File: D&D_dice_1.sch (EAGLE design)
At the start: 29 parts, among them IC1 MCP6282-E/SN-ND, SW1 SPST_SWITCH, SW2 SPST_SWITCH, SW3 SPST_SWITCH, SW4 SPST_SWITCH, SW5 SPST_SWITCH, SW6 SPST_SWITCH, U1 ATMEGA168

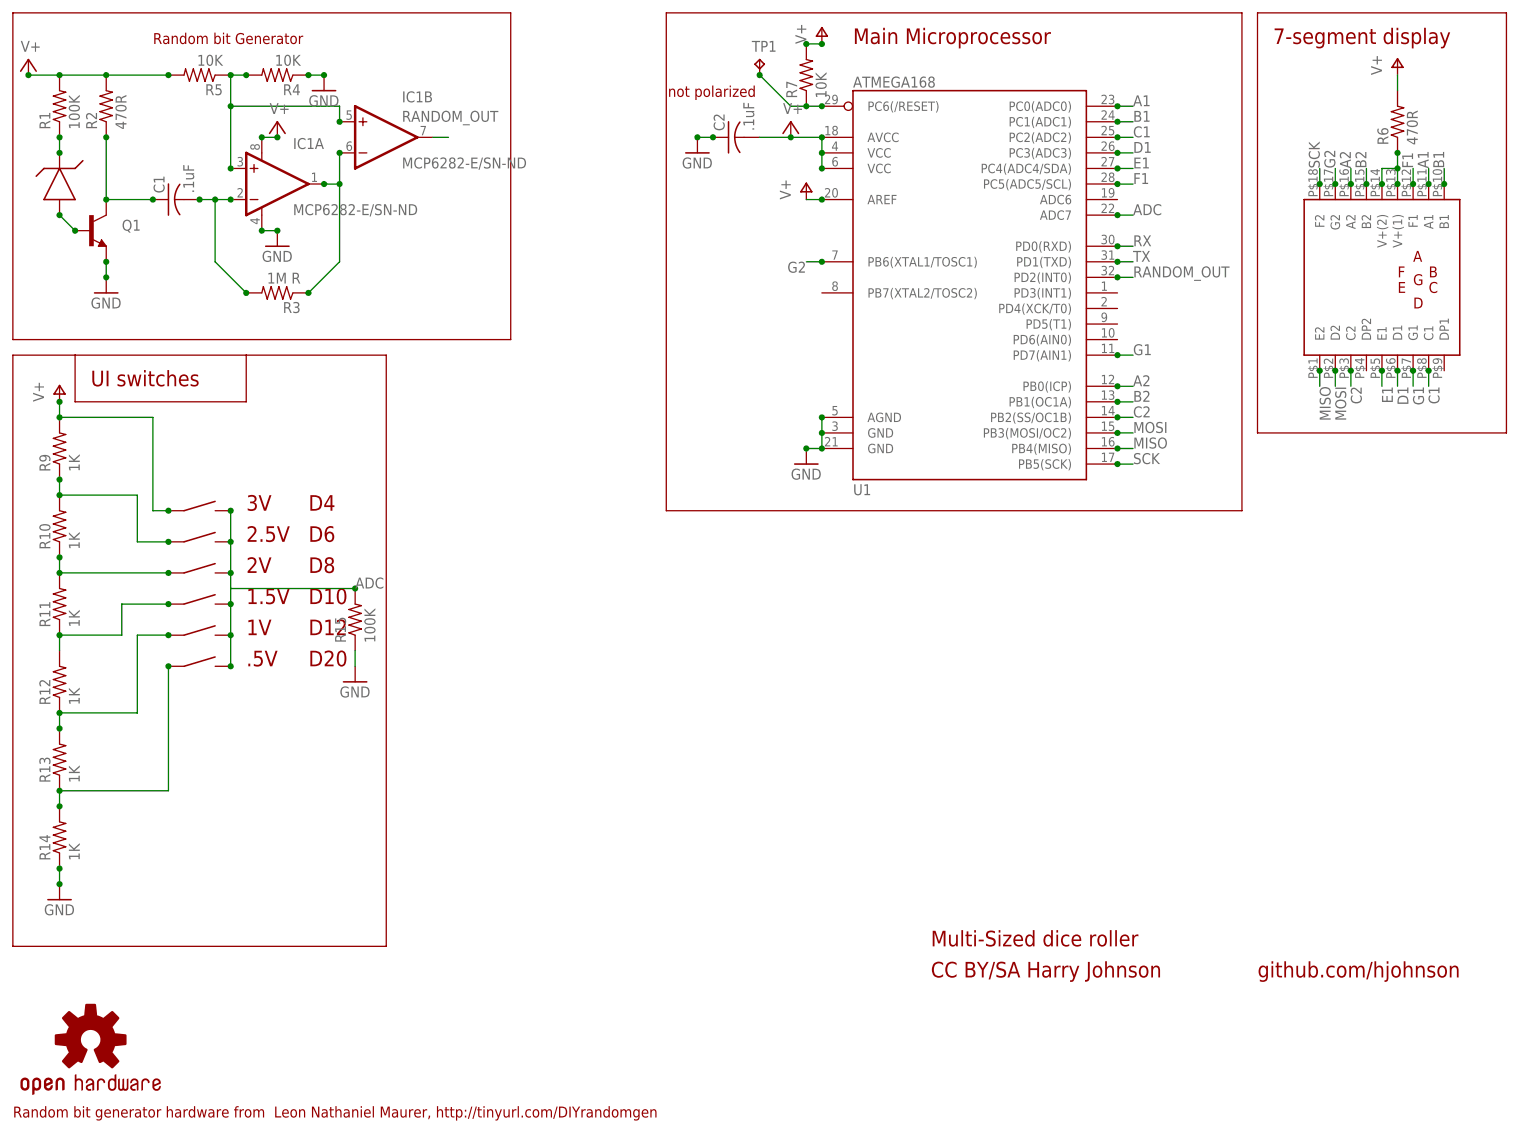
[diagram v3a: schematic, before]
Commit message: Added a whole bunch of explanatory text to the schematic.
Theory of operation, mainly.
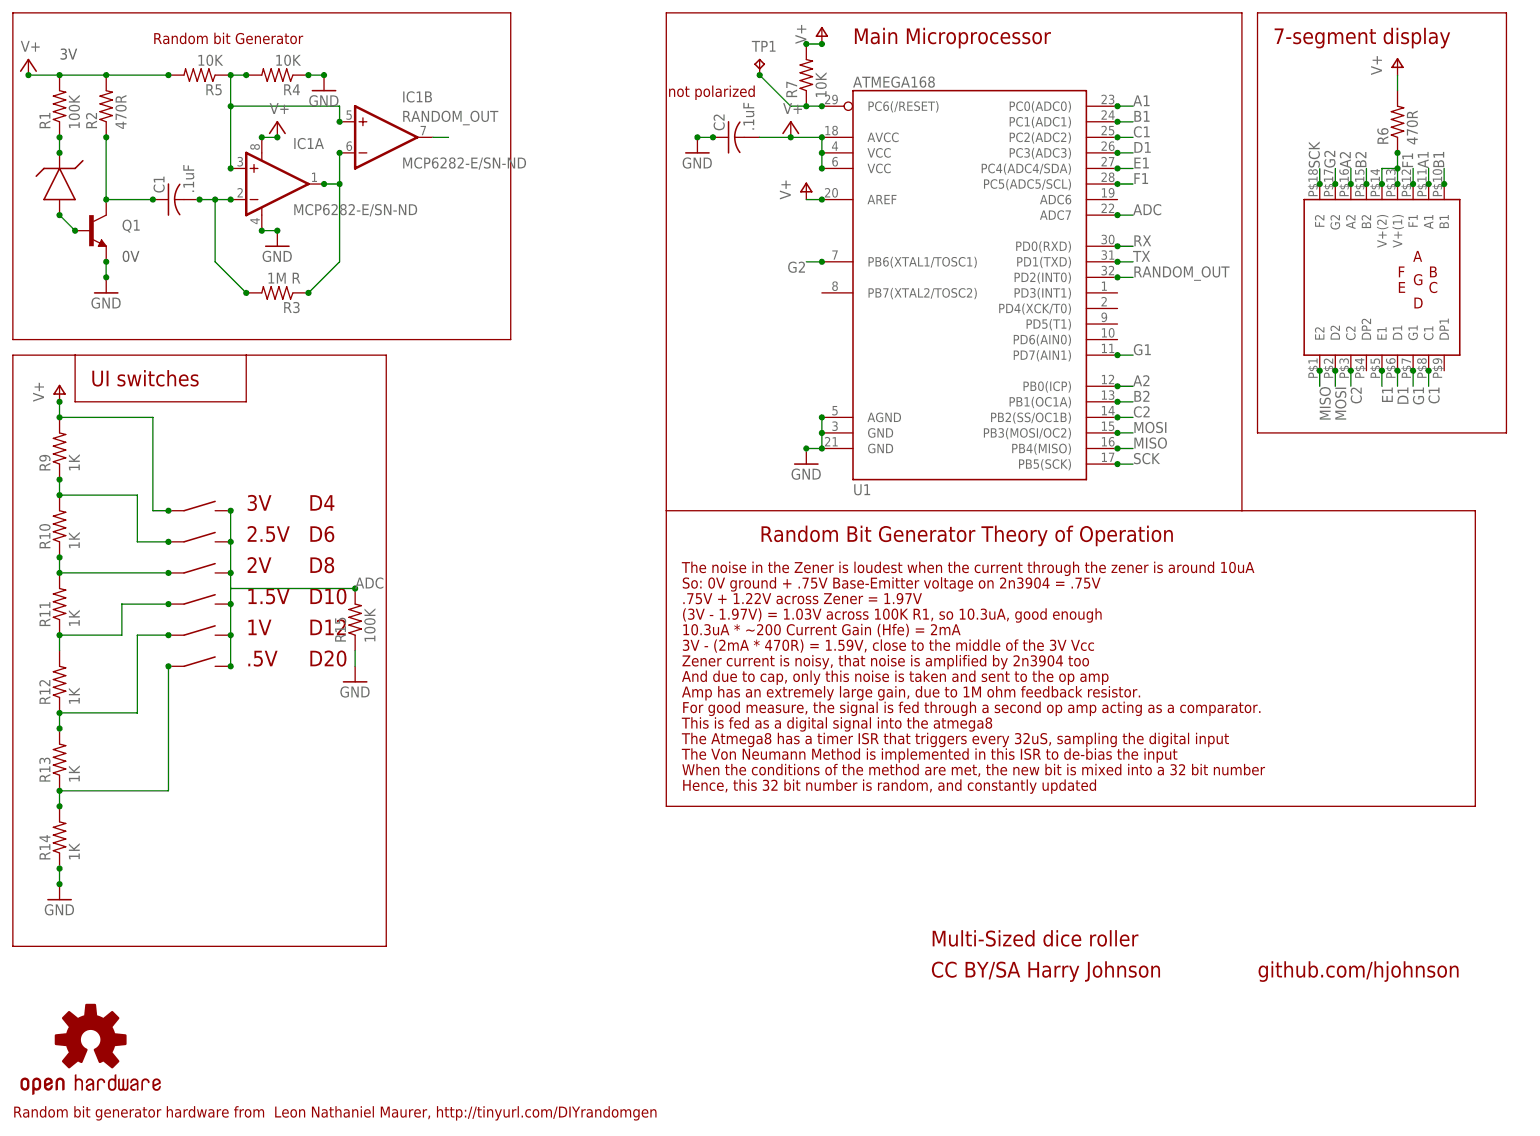
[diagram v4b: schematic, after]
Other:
- note added: "(3V - 1.97V) = 1.03V across 100K R1, so 10.3uA, good enough"
- note added: ".75V + 1.22V across Zener = 1.97V"
- note added: "0V"
- note added: "10.3uA * ~200 Current Gain (Hfe) = 2mA"
- note added: "3V - (2mA * 470R) = 1.59V, close to the middle of the 3V Vcc"
- note added: "Amp has an extremely large gain, due to 1M ohm feedback resistor."
- note added: "And due to cap, only this noise is taken and sent to the op amp"
- note added: "For good measure, the signal is fed through a second op amp acting as a comparator."
- note added: "Hence, this 32 bit number is random, and constantly updated"
- note added: "Random Bit Generator Theory of Operation"
- note added: "So: 0V ground + .75V Base-Emitter voltage on 2n3904 = .75V"
- note added: "The Atmega8 has a timer ISR that triggers every 32uS, sampling the digital input"
- note added: "The Von Neumann Method is implemented in this ISR to de-bias the input"
- note added: "The noise in the Zener is loudest when the current through the zener is around 10uA"
- note added: "This is fed as a digital signal into the atmega8"
- note added: "When the conditions of the method are met, the new bit is mixed into a 32 bit number"
- note added: "Zener current is noisy, that noise is amplified by 2n3904 too"
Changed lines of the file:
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@@
 <text x="152.4" y="25.4" size="2.54" layer="94">CC BY/SA Harry Johnson</text>
 <text x="205.74" y="25.4" size="2.54" layer="94">github.com/hjohnson</text>
+<text x="10.16" y="175.26" size="1.778" layer="97">3V</text>
+<text x="20.32" y="142.24" size="1.778" layer="97">0V</text>
+<text x="124.46" y="96.52" size="2.54" layer="94">Random Bit Generator Theory of Operation</text>
+<text x="111.76" y="91.44" size="1.778" layer="94">The noise in the Zener is loudest when the current through the zener is around 10uA</text>
+<text x="111.76" y="88.9" size="1.778" layer="94">So: 0V ground + .75V Base-Emitter voltage on 2n3904 = .75V</text>
+<text x="111.76" y="86.36" size="1.778" layer="94">.75V + 1.22V across Zener = 1.97V</text>
+<text x="111.76" y="83.82" size="1.778" layer="94">(3V - 1.97V) = 1.03V across 100K R1, so 10.3uA, good enough</text>
+<text x="111.76" y="81.28" size="1.778" layer="94">10.3uA * ~200 Current Gain (Hfe) = 2mA</text>
+<text x="111.76" y="78.74" size="1.778" layer="94">3V - (2mA * 470R) = 1.59V, close to the middle of the 3V Vcc</text>
+<text x="111.76" y="76.2" size="1.778" layer="94">Zener current is noisy, that noise is amplified by 2n3904 too</text>
+<text x="111.76" y="73.66" size="1.778" layer="94">And due to cap, only this noise is taken and sent to the op amp</text>
+<text x="111.76" y="71.12" size="1.778" layer="94">Amp has an extremely large gain, due to 1M ohm feedback resistor.</text>
+<text x="111.76" y="68.58" size="1.778" layer="94">For good measure, the signal is fed through a second op amp acting as a comparator.</text>
+<text x="111.76" y="66.04" size="1.778" layer="94">This is fed as a digital signal into the atmega8</text>
+<text x="111.76" y="63.5" size="1.778" layer="94">The Atmega8 has a timer ISR that triggers every 32uS, sampling the digital input</text>
+<text x="111.76" y="60.96" size="1.778" layer="94">The Von Neumann Method is implemented in this ISR to de-bias the input</text>
+<text x="111.76" y="58.42" size="1.778" layer="94">When the conditions of the method are met, the new bit is mixed into a 32 bit number</text>
+<text x="111.76" y="55.88" size="1.778" layer="94">Hence, this 32 bit number is random, and constantly updated</text>
+<wire x1="109.22" y1="101.6" x2="109.22" y2="53.34" width="0.1524" layer="94"/>
+<wire x1="109.22" y1="53.34" x2="241.3" y2="53.34" width="0.1524" layer="94"/>
+<wire x1="241.3" y1="53.34" x2="241.3" y2="101.6" width="0.1524" layer="94"/>
+<wire x1="241.3" y1="101.6" x2="203.2" y2="101.6" width="0.1524" layer="94"/>
 </plain>
 <instances>

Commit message: Rotated a capacitor to make schematic look better, and added the schematic pdf.
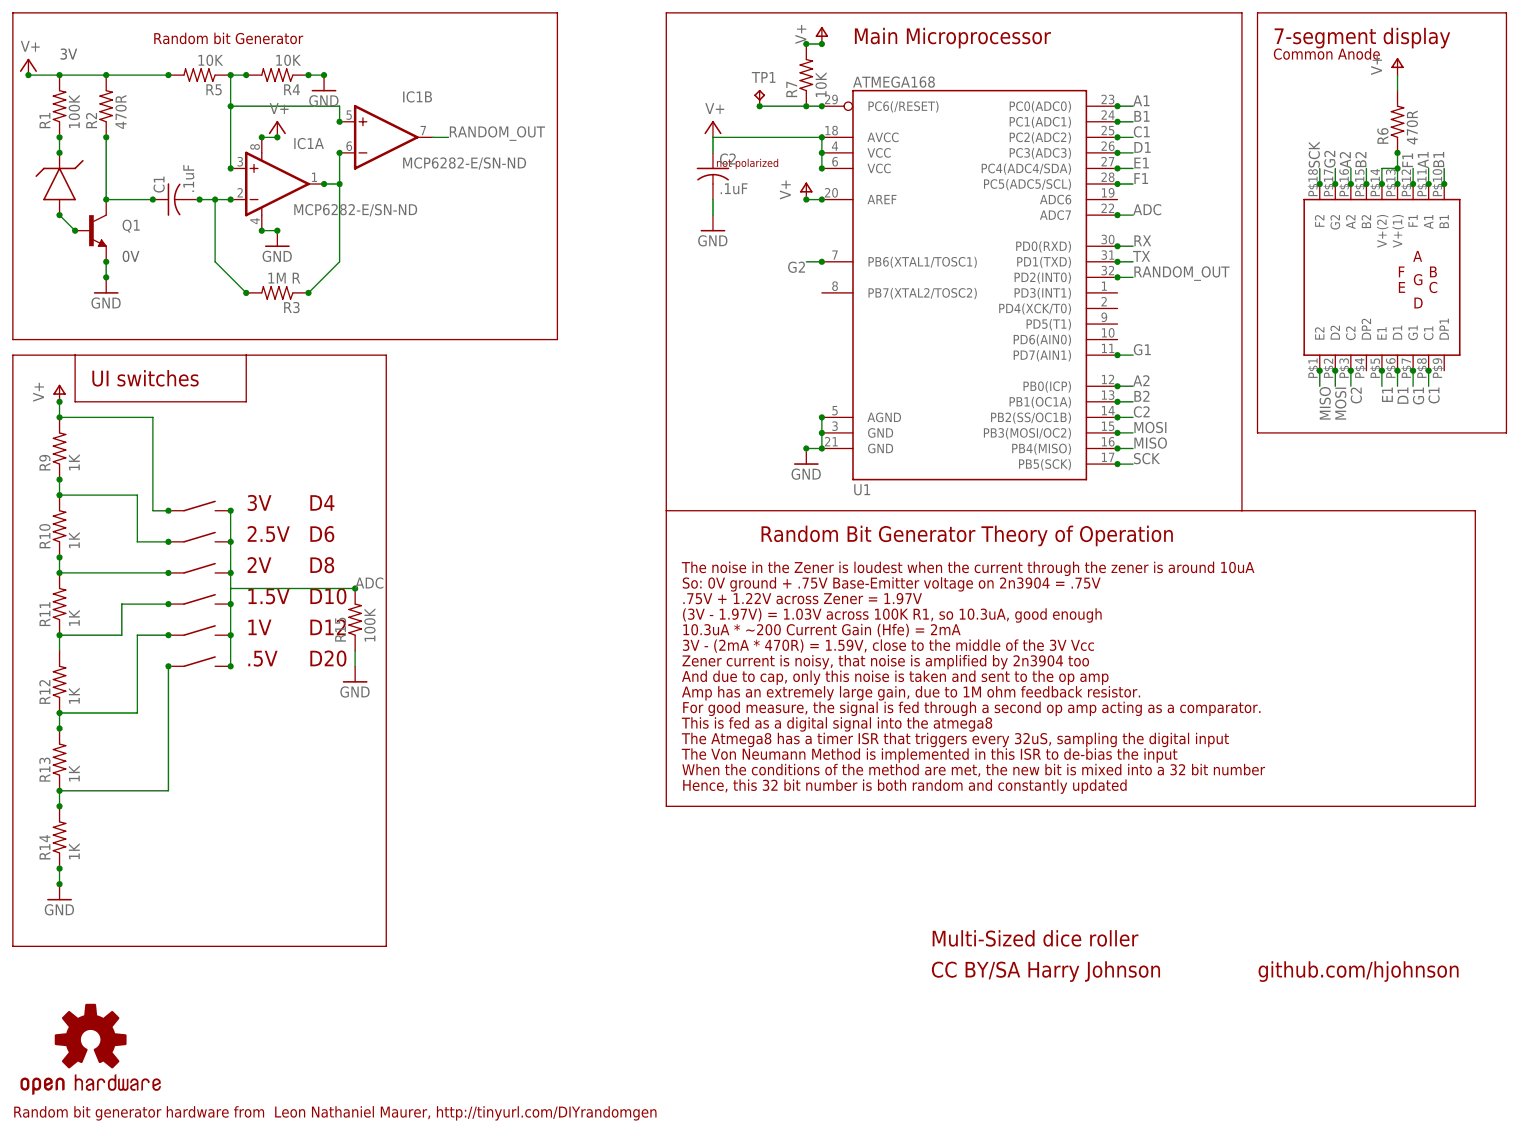
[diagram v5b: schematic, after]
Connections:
- net GND: now also C2.2; no longer C2.1
- net V+: now also C2.1; no longer C2.2
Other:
- note added: "Common Anode"
- note added: "Hence, this 32 bit number is both random and constantly updated"
- note removed: "Hence, this 32 bit number is random, and constantly updated"
- moved on the sheet: C2, TP1
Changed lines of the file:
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@@
 <text x="25.4" y="177.8" size="1.778" layer="94">Random bit Generator</text>
 <wire x1="2.54" y1="182.88" x2="2.54" y2="129.54" width="0.2032" layer="94"/>
-<wire x1="2.54" y1="129.54" x2="83.82" y2="129.54" width="0.2032" layer="94"/>
-<wire x1="83.82" y1="129.54" x2="83.82" y2="182.88" width="0.2032" layer="94"/>
-<wire x1="83.82" y1="182.88" x2="2.54" y2="182.88" width="0.2032" layer="94"/>
+<wire x1="2.54" y1="129.54" x2="91.44" y2="129.54" width="0.2032" layer="94"/>
+<wire x1="91.44" y1="129.54" x2="91.44" y2="182.88" width="0.2032" layer="94"/>
+<wire x1="91.44" y1="182.88" x2="2.54" y2="182.88" width="0.2032" layer="94"/>
 <wire x1="2.54" y1="127" x2="2.54" y2="30.48" width="0.1524" layer="94"/>
 <wire x1="2.54" y1="30.48" x2="63.5" y2="30.48" width="0.1524" layer="94"/>
@@
 <text x="50.8" y="76.2" size="2.54" layer="94">D20</text>
 <text x="2.54" y="2.54" size="1.778" layer="94">Random bit generator hardware from  Leon Nathaniel Maurer, http://tinyurl.com/DIYrandomgen</text>
-<text x="109.474" y="169.164" size="1.778" layer="94">not polarized</text>
+<text x="117.348" y="157.734" size="1.27" layer="94">not polarized</text>
 <text x="152.4" y="30.48" size="2.54" layer="94">Multi-Sized dice roller</text>
 <text x="152.4" y="25.4" size="2.54" layer="94">CC BY/SA Harry Johnson</text>
@@
 <text x="111.76" y="60.96" size="1.778" layer="94">The Von Neumann Method is implemented in this ISR to de-bias the input</text>
 <text x="111.76" y="58.42" size="1.778" layer="94">When the conditions of the method are met, the new bit is mixed into a 32 bit number</text>
-<text x="111.76" y="55.88" size="1.778" layer="94">Hence, this 32 bit number is random, and constantly updated</text>
+<text x="111.76" y="55.88" size="1.778" layer="94">Hence, this 32 bit number is both random and constantly updated</text>
 <wire x1="109.22" y1="101.6" x2="109.22" y2="53.34" width="0.1524" layer="94"/>
 <wire x1="109.22" y1="53.34" x2="241.3" y2="53.34" width="0.1524" layer="94"/>
 <wire x1="241.3" y1="53.34" x2="241.3" y2="101.6" width="0.1524" layer="94"/>
 <wire x1="241.3" y1="101.6" x2="203.2" y2="101.6" width="0.1524" layer="94"/>
+<text x="208.28" y="175.26" size="1.778" layer="94">Common Anode</text>
 </plain>
 <instances>
@@
 <instance part="R5" gate="G$1" x="33.02" y="172.72" rot="R180"/>
 <instance part="C1" gate="G$1" x="27.94" y="152.4" rot="R90"/>
-<instance part="C2" gate="G$1" x="119.38" y="162.56" rot="R90"/>
+<instance part="C2" gate="G$1" x="116.84" y="157.48"/>
 <instance part="U1" gate="G$1" x="157.48" y="142.24"/>
 <instance part="U$2" gate="G$1" x="226.06" y="139.7"/>
@@
 <instance part="SUPPLY1" gate="1" x="5.08" y="175.26"/>
 <instance part="SUPPLY2" gate="1" x="45.72" y="165.1"/>
-<instance part="SUPPLY3" gate="1" x="129.54" y="165.1"/>
+<instance part="SUPPLY3" gate="1" x="116.84" y="165.1"/>
 <instance part="GND3" gate="1" x="132.08" y="109.22"/>
 <instance part="R6" gate="G$1" x="228.6" y="165.1" rot="R90"/>
 <instance part="P+1" gate="1" x="228.6" y="175.26"/>
-<instance part="GND4" gate="1" x="114.3" y="160.02"/>
+<instance part="GND4" gate="1" x="116.84" y="147.32"/>
 <instance part="R7" gate="G$1" x="132.08" y="172.72" rot="R90"/>
 <instance part="P+3" gate="1" x="134.62" y="180.34"/>
@@
 <instance part="R15" gate="G$1" x="58.42" y="83.82" rot="R90"/>
 <instance part="GND7" gate="1" x="58.42" y="73.66"/>
-<instance part="TP1" gate="G$1" x="124.46" y="175.26"/>
+<instance part="TP1" gate="G$1" x="124.46" y="170.18"/>
 </instances>
 <busses>
@@
 </segment>
 <segment>
-<pinref part="GND4" gate="1" pin="GND"/>
-<pinref part="C2" gate="G$1" pin="1"/>
-<wire x1="114.3" y1="162.56" x2="116.84" y2="162.56" width="0.1524" layer="91"/>
-<junction x="116.84" y="162.56"/>
-<junction x="114.3" y="162.56"/>
-</segment>
-<segment>
 <pinref part="GND5" gate="1" pin="GND"/>
 <wire x1="10.16" y1="43.18" x2="10.16" y2="40.64" width="0.1524" layer="91"/>
@@
 <pinref part="GND7" gate="1" pin="GND"/>
 <wire x1="58.42" y1="78.74" x2="58.42" y2="76.2" width="0.1524" layer="91"/>
+</segment>
+<segment>
+<pinref part="GND4" gate="1" pin="GND"/>
+<pinref part="C2" gate="G$1" pin="2"/>
+<wire x1="116.84" y1="152.4" x2="116.84" y2="149.86" width="0.1524" layer="91"/>
 </segment>
 </net>
@@
 <pinref part="SUPPLY3" gate="1" pin="V+"/>
 <pinref part="U1" gate="G$1" pin="AVCC"/>
-<wire x1="129.54" y1="162.56" x2="134.62" y2="162.56" width="0.1524" layer="91"/>
+<wire x1="116.84" y1="162.56" x2="134.62" y2="162.56" width="0.1524" layer="91"/>
 <pinref part="U1" gate="G$1" pin="VCC@1"/>
 <wire x1="134.62" y1="162.56" x2="134.62" y2="160.02" width="0.1524" layer="91"/>
 <pinref part="U1" gate="G$1" pin="VCC@2"/>
 <wire x1="134.62" y1="160.02" x2="134.62" y2="157.48" width="0.1524" layer="91"/>
-<pinref part="C2" gate="G$1" pin="2"/>
-<wire x1="124.46" y1="162.56" x2="129.54" y2="162.56" width="0.1524" layer="91"/>
 <junction x="134.62" y="162.56"/>
 <junction x="134.62" y="160.02"/>
 <junction x="134.62" y="157.48"/>
-<junction x="129.54" y="162.56"/>
+<pinref part="C2" gate="G$1" pin="1"/>
+<wire x1="116.84" y1="162.56" x2="116.84" y2="160.02" width="0.1524" layer="91"/>
 </segment>
 <segment>
@@
 <wire x1="132.08" y1="152.4" x2="134.62" y2="152.4" width="0.1524" layer="91"/>
 <junction x="134.62" y="152.4"/>
+<junction x="132.08" y="152.4"/>
 </segment>
 </net>
@@
 <junction x="134.62" y="167.64"/>
 <pinref part="TP1" gate="G$1" pin="TP"/>
-<wire x1="124.46" y1="172.72" x2="129.54" y2="167.64" width="0.1524" layer="91"/>
-<wire x1="129.54" y1="167.64" x2="132.08" y2="167.64" width="0.1524" layer="91"/>
-<junction x="124.46" y="172.72"/>
+<wire x1="124.46" y1="167.64" x2="132.08" y2="167.64" width="0.1524" layer="91"/>
+<junction x="124.46" y="167.64"/>
 </segment>
 </net>
@@
 <pinref part="IC1" gate="B" pin="OUT"/>
 <wire x1="71.12" y1="162.56" x2="73.66" y2="162.56" width="0.1524" layer="91"/>
-<label x="66.04" y="165.1" size="1.778" layer="95"/>
-</segment>
-<segment>
+<label x="73.66" y="162.56" size="1.778" layer="95"/>
+</segment>
+<segment>
